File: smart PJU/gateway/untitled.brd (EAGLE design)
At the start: 80 x 80 mm, 43 parts, among them J1 U.FL-R-SMT(01), J2 10118193-0001LF, Q16 MMBT3904, Q17 MMBT3904, Q18 12MHz, U1 AMS1117, U19 CH340G

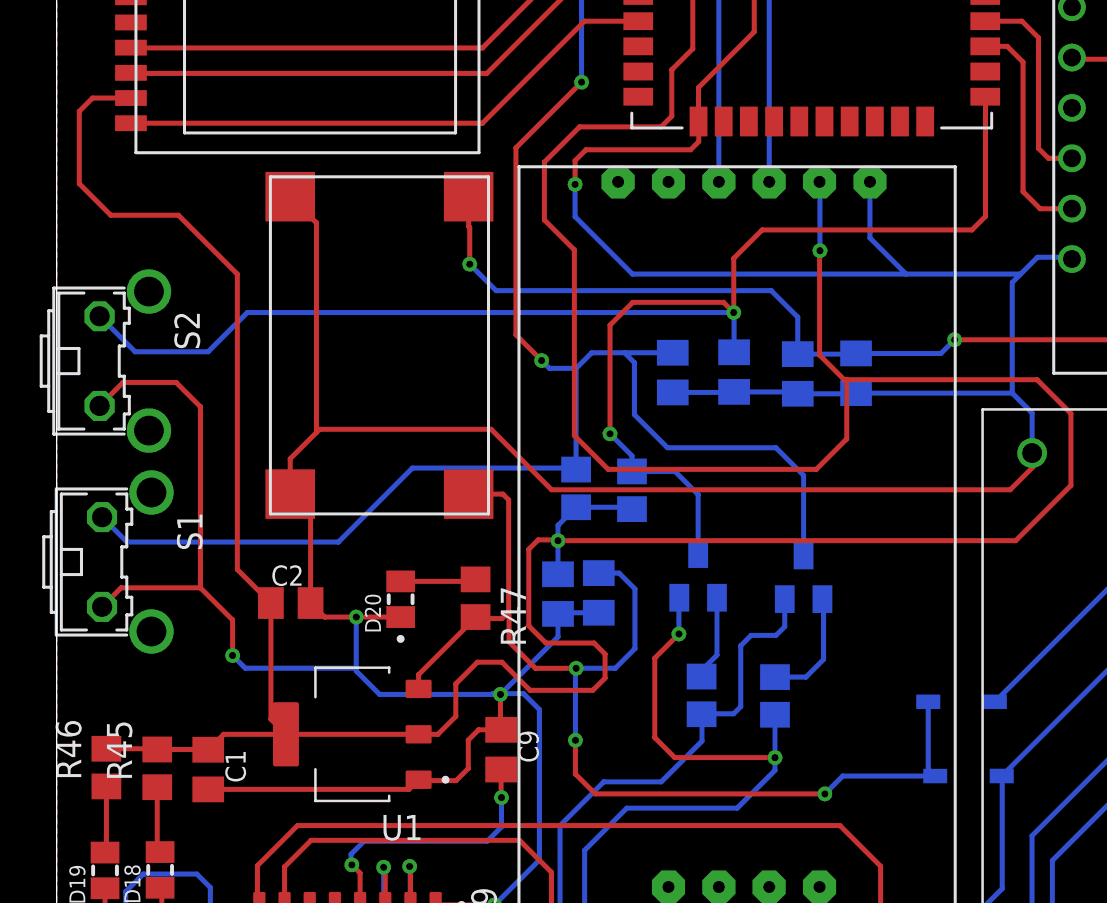
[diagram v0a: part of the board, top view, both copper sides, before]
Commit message: revisi relay node dan list komponen
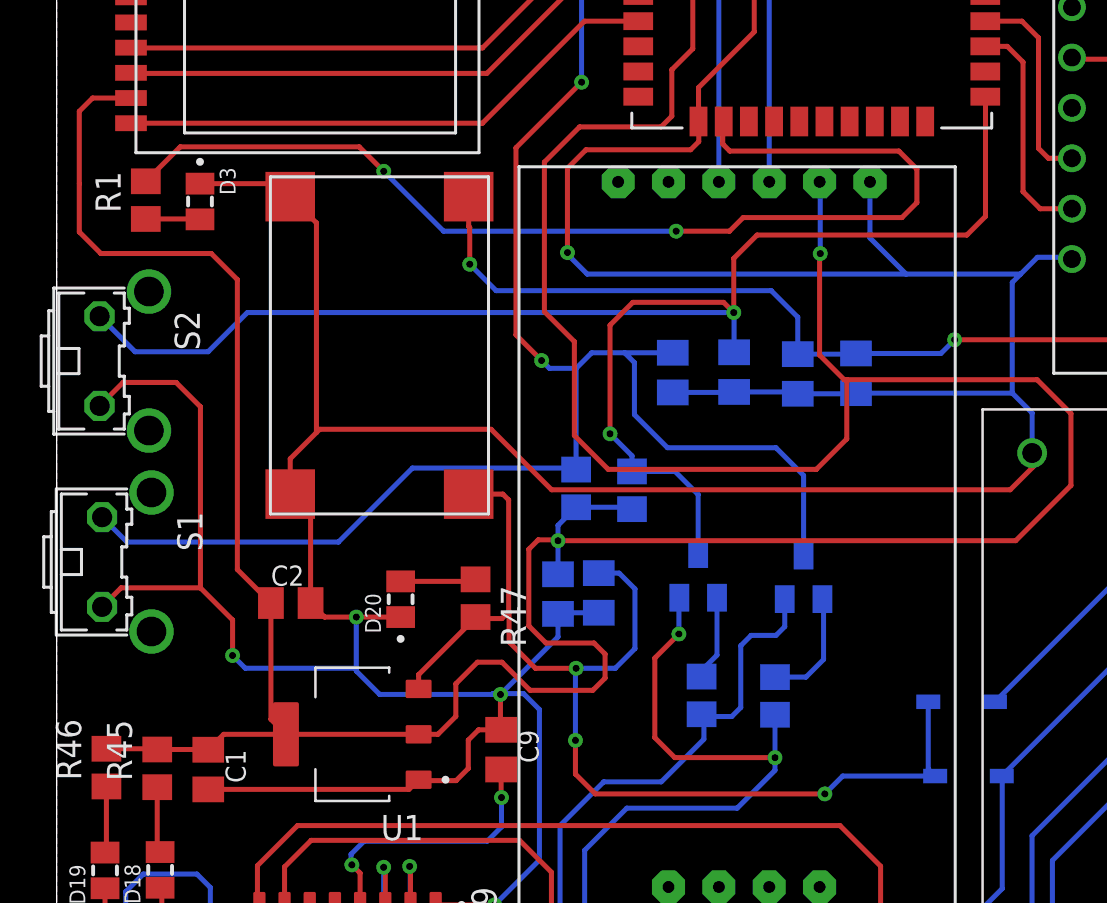
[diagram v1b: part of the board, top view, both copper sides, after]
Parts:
- added D3: SML-LXT0805IW-TR, SML-LXT0805IW-TR:LEDC2012X120N
- added R1: 10k, rcl:R0805
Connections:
- new net LED-LORA: MD1.16, R1.2
- new net N$7: D3.A, R1.1
- net GND: now also D3.C
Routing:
- net LED-LORA: track 0.00 -> 55.1 mm, vias 0 -> 2
- net GND: track 391.4 -> 397.8 mm
- net N$7: track 0.00 -> 3.06 mm
- net 3V3: track 199.2 -> 200.5 mm

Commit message: revisi PS hilink 2A
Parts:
- removed PS1: HLK-5M05, HLK-5M05:CONV_HLK-5M05
- added PS2: HLK-10M05, HLK-10M05:HLK10M05
- moved C15 61.6 mm to (4.91, 75.9), turned to 180 degrees
- moved C8 59.5 mm to (13.6, 75.9), turned to 0 degrees
- moved TB7.1 39.7 mm to (76.8, 56.4)
- moved SIM800L1 13.2 mm to (66.9, 57.1), turned to 180 degrees
- moved J1 2.88 mm to (20.4, 75.5)
- moved MD1 0.41 mm to (37.7, 66.1)
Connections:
- net GND: now also PS2.3; no longer PS1.3
- net N$1: now also PS2.1; no longer PS1.1
- net N$2: now also PS2.2; no longer PS1.2
- net N$3: now also PS2.4; no longer PS1.4
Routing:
- net VCC_USB: track 136.7 -> 189.3 mm, vias 3 -> 5
- net N$2: track 51.1 -> 91.2 mm
- net N$1: track 44.4 -> 80.3 mm
- net RX: track 199.9 -> 167.2 mm
- net TX: track 184.1 -> 155.5 mm
- net N$5: track 80.9 -> 105.1 mm, vias 2 -> 3
- net TX_SIM: track 11.6 -> 34.4 mm
- net RX_SIM: track 10.5 -> 31.2 mm, vias 0 -> 1
- net N$3: track 25.7 -> 42.2 mm, vias 0 -> 1
- net MISO_VSPI: track 70.3 -> 66.6 mm, vias 0 -> 2
- net SCK_VSPI: track 74.5 -> 71.3 mm, vias 0 -> 2
- net ANT: track 6.38 -> 4.03 mm
- net GND: track 397.8 -> 399.5 mm
- net SS_LORA: track 62.9 -> 64.4 mm
- removed copper zone on layer 1, net N$4
- removed copper zone on layer 16, net N$6

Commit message: revisi rangkaian
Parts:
- moved SIM800L1 23.5 mm to (54.5, 77.1), turned to 0 degrees
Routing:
- net RX_SIM: track 31.2 -> 7.77 mm, vias 1 -> 0
- net TX_SIM: track 34.4 -> 12.6 mm
- net N$5: track 105.1 -> 109.7 mm
- net GND: track 399.5 -> 398.4 mm, vias 9 -> 10
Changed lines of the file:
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@@
 <attribute name="VALUE" x="-2.55784375" y="48.356021875" size="1.27" layer="27" ratio="10" rot="R270"/>
 </element>
-<element name="SIM800L1" library="sim800l" package="SIM800L" value="" x="66.8797375" y="57.124475" smashed="yes" rot="R180"/>
+<element name="SIM800L1" library="sim800l" package="SIM800L" value="" x="54.480215625" y="77.1257875" smashed="yes"/>
 <element name="TB7.1" library="TB7.62" package="TB7.62" value="" x="76.7798875" y="56.35535" smashed="yes" rot="R90"/>
 <element name="U1" library="AMS1117" package="SOT229P700X180-4N" value="AMS1117" x="14.909628125" y="25.8509125" smashed="yes" rot="R180">
@@
 <wire x1="18.9179625" y1="70.7185625" x2="18.9179625" y2="75.529778125" width="0.254" layer="1"/>
 <wire x1="20.087925" y1="69.5486" x2="18.9179625" y2="70.7185625" width="0.254" layer="1"/>
-<wire x1="71.9597375" y1="72.364475" x2="71.9597375" y2="74.052496875" width="0.254" layer="1"/>
-<wire x1="71.9597375" y1="74.052496875" x2="69.717171875" y2="76.2950625" width="0.254" layer="1"/>
-<wire x1="69.717171875" y1="76.2950625" x2="47.41671875" y2="76.2950625" width="0.254" layer="1"/>
-<wire x1="47.41671875" y1="76.2950625" x2="46.420396875" y2="75.298740625" width="0.254" layer="1"/>
-<wire x1="46.420396875" y1="75.298740625" x2="46.420396875" y2="74.463625" width="0.254" layer="1"/>
 <wire x1="48.76163125" y1="47.51895" x2="48.76163125" y2="42.789946875" width="0.254" layer="16"/>
 <wire x1="48.76163125" y1="42.789946875" x2="47.663540625" y2="41.69185625" width="0.254" layer="16"/>
@@
 <wire x1="20.3246375" y1="77.73741875" x2="20.3246375" y2="77.7075625" width="0.254" layer="16"/>
 <via x="20.3246375" y="77.7075625" extent="1-16" drill="0.35"/>
+<wire x1="49.400215625" y1="61.8857875" x2="53.821265625" y2="61.8857875" width="0.254" layer="16"/>
+<wire x1="53.821265625" y1="61.8857875" x2="54.9566" y2="63.021121875" width="0.254" layer="16"/>
+<wire x1="54.9566" y1="63.021121875" x2="54.9566" y2="74.737590625" width="0.254" layer="16"/>
+<wire x1="54.9566" y1="74.737590625" x2="52.751184375" y2="76.94300625" width="0.254" layer="16"/>
+<wire x1="52.751184375" y1="76.94300625" x2="49.264240625" y2="76.94300625" width="0.254" layer="16"/>
+<wire x1="49.264240625" y1="76.94300625" x2="49.264240625" y2="76.913196875" width="0.254" layer="16"/>
+<via x="49.264240625" y="76.913196875" extent="1-16" drill="0.35"/>
+<wire x1="49.264240625" y1="76.913196875" x2="48.86996875" y2="76.913196875" width="0.254" layer="1"/>
+<wire x1="48.86996875" y1="76.913196875" x2="46.420396875" y2="74.463625" width="0.254" layer="1"/>
 </signal>
 <signal name="SCK_VSPI">
@@
 <wire x1="56.26163125" y1="5.01895" x2="56.26163125" y2="8.022496875" width="1.27" layer="16"/>
 <wire x1="56.26163125" y1="8.022496875" x2="64.550153125" y2="16.31101875" width="1.27" layer="16"/>
-<wire x1="64.550153125" y1="16.31101875" x2="64.550153125" y2="47.425615625" width="1.27" layer="16"/>
-<wire x1="64.550153125" y1="47.425615625" x2="77.3798875" y2="60.25535" width="1.27" layer="16"/>
+<wire x1="64.550153125" y1="16.31101875" x2="64.550153125" y2="46.82454375" width="1.27" layer="16"/>
+<wire x1="77.3798875" y1="59.654278125" x2="64.550153125" y2="46.82454375" width="1.27" layer="16"/>
+<wire x1="77.3798875" y1="59.654278125" x2="77.3798875" y2="60.25535" width="1.27" layer="16"/>
 </signal>
 <signal name="N$2">
@@
 <contactref element="MD1" pad="27"/>
 <contactref element="SIM800L1" pad="TXD"/>
-<wire x1="46.420396875" y1="60.493625" x2="47.3627" y2="60.493625" width="0.254" layer="1"/>
-<wire x1="47.3627" y1="60.493625" x2="50.974603125" y2="56.881721875" width="0.254" layer="1"/>
-<wire x1="50.974603125" y1="56.881721875" x2="60.237478125" y2="56.881721875" width="0.254" layer="1"/>
-<wire x1="60.237478125" y1="56.881721875" x2="68.6922875" y2="65.33653125" width="0.254" layer="1"/>
-<wire x1="68.6922875" y1="65.33653125" x2="68.6922875" y2="68.823746875" width="0.254" layer="1"/>
-<wire x1="69.693015625" y1="69.824475" x2="71.9597375" y2="69.824475" width="0.254" layer="1"/>
-<wire x1="69.693015625" y1="69.824475" x2="68.6922875" y2="68.823746875" width="0.254" layer="1"/>
+<wire x1="49.400215625" y1="64.4257875" x2="50.823984375" y2="64.4257875" width="0.254" layer="1"/>
+<wire x1="50.823984375" y1="64.4257875" x2="51.67513125" y2="63.574640625" width="0.254" layer="1"/>
+<wire x1="51.67513125" y1="63.574640625" x2="51.67513125" y2="59.725396875" width="0.254" layer="1"/>
+<wire x1="51.67513125" y1="59.725396875" x2="51.074978125" y2="59.12524375" width="0.254" layer="1"/>
+<wire x1="51.074978125" y1="59.12524375" x2="49.419384375" y2="59.12524375" width="0.254" layer="1"/>
+<wire x1="49.419384375" y1="59.12524375" x2="48.053525" y2="60.491103125" width="0.254" layer="1"/>
+<wire x1="48.053525" y1="60.491103125" x2="47.14295" y2="60.491103125" width="0.254" layer="1"/>
+<wire x1="47.14295" y1="60.491103125" x2="47.12225625" y2="60.470409375" width="0.254" layer="1"/>
+<wire x1="47.12225625" y1="60.470409375" x2="46.4436125" y2="60.470409375" width="0.254" layer="1"/>
+<wire x1="46.4436125" y1="60.470409375" x2="46.420396875" y2="60.493625" width="0.254" layer="1"/>
 </signal>
 <signal name="RX_SIM">
 <contactref element="MD1" pad="28"/>
 <contactref element="SIM800L1" pad="RXD"/>
-<wire x1="46.420396875" y1="61.763625" x2="47.10725625" y2="61.763625" width="0.254" layer="1"/>
-<wire x1="47.10725625" y1="61.763625" x2="51.11418125" y2="57.7567" width="0.254" layer="1"/>
-<wire x1="51.11418125" y1="57.7567" x2="58.860425" y2="57.7567" width="0.254" layer="1"/>
-<wire x1="58.860425" y1="57.7567" x2="67.395753125" y2="66.292028125" width="0.254" layer="1"/>
-<via x="67.395753125" y="66.292028125" extent="1-16" drill="0.35"/>
-<wire x1="68.353971875" y1="67.284475" x2="67.395753125" y2="66.32625625" width="0.254" layer="16"/>
-<wire x1="67.395753125" y1="66.292028125" x2="67.395753125" y2="66.32625625" width="0.254" layer="16"/>
-<wire x1="68.353971875" y1="67.284475" x2="71.9597375" y2="67.284475" width="0.254" layer="16"/>
+<wire x1="49.400215625" y1="66.9657875" x2="48.368453125" y2="66.9657875" width="0.254" layer="1"/>
+<wire x1="48.368453125" y1="66.9657875" x2="47.930621875" y2="66.52795625" width="0.254" layer="1"/>
+<wire x1="47.930621875" y1="66.52795625" x2="47.930621875" y2="62.025696875" width="0.254" layer="1"/>
+<wire x1="47.66855" y1="61.763625" x2="46.420396875" y2="61.763625" width="0.254" layer="1"/>
+<wire x1="47.930621875" y1="62.025696875" x2="47.66855" y2="61.763625" width="0.254" layer="1"/>
 </signal>
 <signal name="N$5">
@@
 <wire x1="20.77915625" y1="51.4611875" x2="20.77915625" y2="52.964640625" width="0.254" layer="1"/>
 <wire x1="20.832628125" y1="51.407715625" x2="20.77915625" y2="51.4611875" width="0.254" layer="1"/>
-<wire x1="40.31340625" y1="45.055684375" x2="45.378440625" y2="45.055684375" width="0.254" layer="16"/>
-<wire x1="45.378440625" y1="45.055684375" x2="45.391884375" y2="45.069128125" width="0.254" layer="16"/>
-<via x="45.391884375" y="45.069128125" extent="1-16" drill="0.35"/>
-<wire x1="45.391884375" y1="45.069128125" x2="54.074334375" y2="45.069128125" width="0.254" layer="1"/>
 <wire x1="20.832625" y1="49.556759375" x2="9.919903125" y2="49.556759375" width="0.254" layer="16"/>
 <wire x1="2.5149875" y1="56.961675" x2="2.5149875" y2="73.046078125" width="0.254" layer="16"/>
@@
 <wire x1="2.5149875" y1="75.743009375" x2="2.712175" y2="75.940196875" width="0.254" layer="1"/>
 <wire x1="9.919903125" y1="49.556759375" x2="2.5149875" y2="56.961675" width="0.254" layer="16"/>
-<wire x1="71.20968125" y1="62.204475" x2="54.074334375" y2="45.069128125" width="0.254" layer="1"/>
-<wire x1="71.9597375" y1="62.204475" x2="71.20968125" y2="62.204475" width="0.254" layer="1"/>
+<wire x1="49.400215625" y1="72.0457875" x2="52.4696375" y2="72.0457875" width="0.254" layer="1"/>
+<wire x1="52.4696375" y1="72.0457875" x2="54.177784375" y2="70.337640625" width="0.254" layer="1"/>
+<wire x1="54.177784375" y1="70.337640625" x2="54.177784375" y2="47.6766875" width="0.254" layer="1"/>
+<wire x1="54.177784375" y1="47.6766875" x2="51.704103125" y2="45.20300625" width="0.254" layer="1"/>
+<wire x1="51.704103125" y1="45.20300625" x2="43.086784375" y2="45.20300625" width="0.254" layer="1"/>
+<wire x1="43.086784375" y1="45.20300625" x2="42.81358125" y2="45.476209375" width="0.254" layer="1"/>
+<via x="42.81358125" y="45.476209375" extent="1-16" drill="0.35"/>
+<wire x1="42.81358125" y1="45.476209375" x2="40.73393125" y2="45.476209375" width="0.254" layer="16"/>
+<wire x1="40.73393125" y1="45.476209375" x2="40.31340625" y2="45.055684375" width="0.254" layer="16"/>
 </signal>
 <signal name="LED-LORA">
